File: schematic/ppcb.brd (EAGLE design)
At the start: 31.8 x 36.8 mm, 14 parts, among them U1 ATTINY*5, U2 LM211N

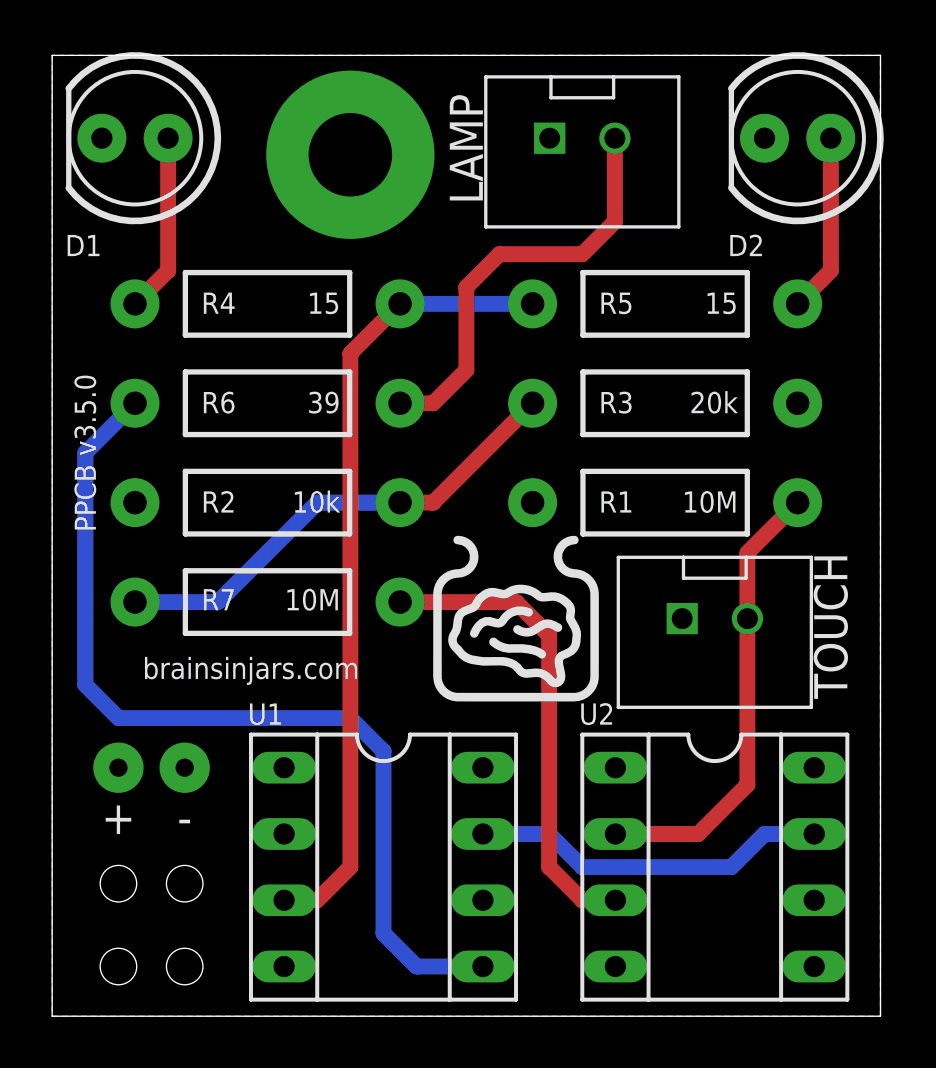
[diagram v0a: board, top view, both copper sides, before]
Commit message: Updated PCB to remove external analog comparator and make use of Timer/Counter-1 instead of Timer/Counter-0
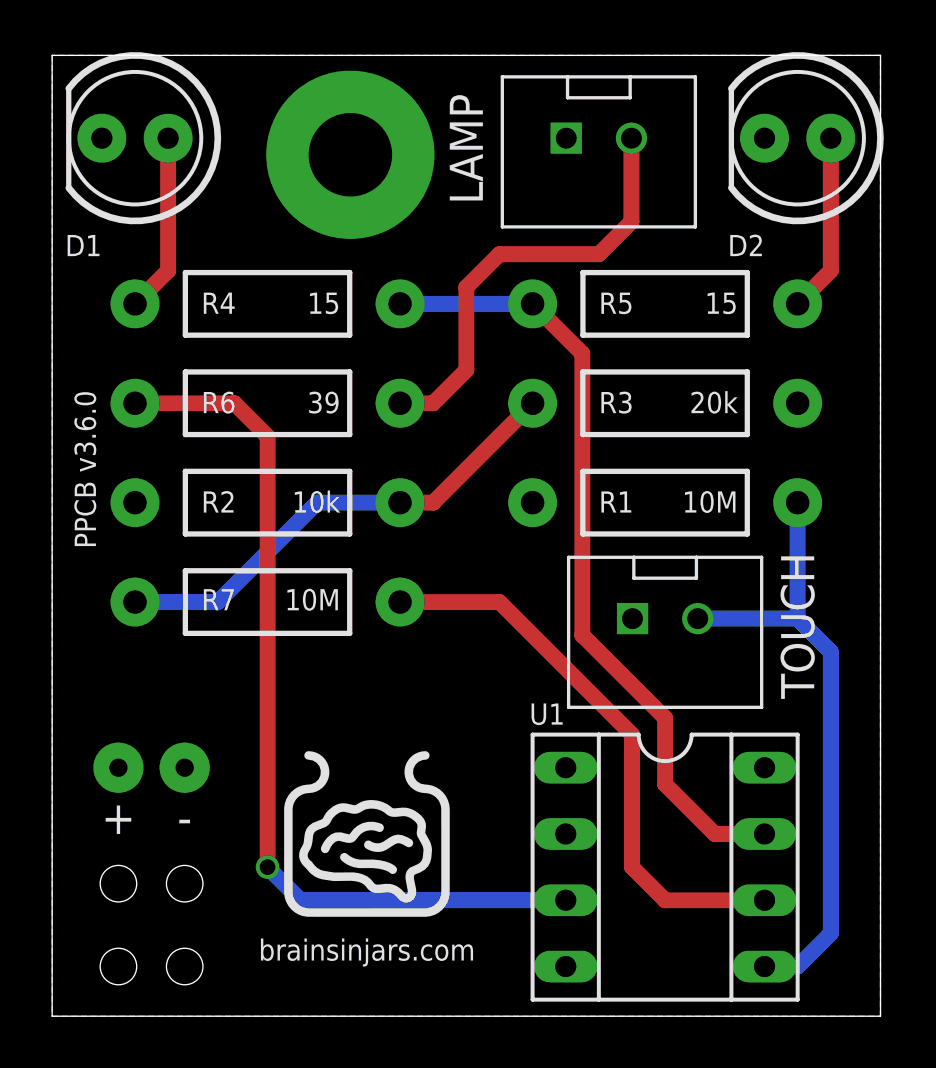
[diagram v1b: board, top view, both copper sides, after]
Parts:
- removed U2: LM211N, ic-package:SOCKET-08
- moved U1 10.8 mm to (23.5, 5.71)
- moved U$2 10.0 mm to (12.1, 6.99)
- moved SW 1.90 mm to (23.5, 15.2)
- moved LED 0.63 mm to (21.0, 33.7)
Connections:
- removed net TOUCH: U1.7, U2.7
- net N$1: now also U1.5; no longer U2.2
- net N$2: now also R7.P$2, U1.6; no longer R6.P$1, U1.5
- net N$7: now also R6.P$1, U1.3; no longer R7.P$2, U2.3
- net N$9: now also U1.7; no longer U1.3
- net V+: no longer U2.8
- net V-: no longer U2.1, U2.4
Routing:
- net N$7: track 18.2 -> 34.1 mm, vias 0 -> 1
- net TOUCH: track 13.8 -> 0.00 mm
- net N$2: track 35.4 -> 21.7 mm
- net N$1: track 17.5 -> 23.9 mm
- net N$3: track 16.2 -> 16.8 mm
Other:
- board text added: "PPCB v3.6.0"
- board text removed: "PPCB v3.5.0"
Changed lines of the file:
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@@
 <hole x="2.54" y="1.905" drill="1.4"/>
 <hole x="5.08" y="1.905" drill="1.4"/>
-<text x="7.62" y="13.335" size="0.8128" layer="21" font="vector" ratio="15" rot="R180" align="center">brainsinjars.com</text>
+<text x="12.065" y="2.54" size="0.8128" layer="21" font="vector" ratio="15" rot="R180" align="center">brainsinjars.com</text>
 <text x="16.51" y="31.115" size="1.27" layer="21" ratio="15" rot="R90">LAMP</text>
-<text x="29.21" y="17.78" size="1.27" layer="21" ratio="15" rot="R270">TOUCH</text>
-<text x="1.27" y="21.59" size="0.8128" layer="21" font="vector" ratio="15" rot="R90" align="center">PPCB v3.5.0</text>
+<text x="27.94" y="17.78" size="1.27" layer="21" ratio="15" rot="R270">TOUCH</text>
+<text x="1.27" y="20.955" size="0.8128" layer="21" font="vector" ratio="15" rot="R270" align="center">PPCB v3.6.0</text>
 </plain>
 <attributes>
@@
 </autorouter>
 <elements>
-<element name="LED" library="con-jst-xh" package="B2B-XH" value="02-JST" x="20.32" y="33.655"/>
-<element name="SW" library="con-jst-xh" package="B2B-XH" value="02-JST" x="25.4" y="15.24"/>
-<element name="U$2" library="brainsinjars" package="LOGO-1_4_IN" value="" x="17.78" y="15.24"/>
+<element name="LED" library="con-jst-xh" package="B2B-XH" value="02-JST" x="20.955" y="33.655"/>
+<element name="SW" library="con-jst-xh" package="B2B-XH" value="02-JST" x="23.495" y="15.24"/>
+<element name="U$2" library="brainsinjars" package="LOGO-1_4_IN" value="" x="12.065" y="6.985"/>
 <element name="R4" library="SparkFun-Resistors" package="AXIAL-0.4" value="15" x="8.255" y="27.305" smashed="yes">
 <attribute name="NAME" x="5.715" y="26.924" size="0.8128" layer="25" font="vector" ratio="15"/>
@@
 <attribute name="VALUE" x="25.3746" y="35.4584" size="1.27" layer="27" ratio="10" rot="R180"/>
 </element>
-<element name="U1" library="ic-package" package="SOCKET-08" value="ATTINY*5" x="12.7" y="5.715" smashed="yes" rot="R270">
-<attribute name="VALUE" x="12.192" y="8.763" size="1.27" layer="27" ratio="10" rot="R270"/>
-<attribute name="NAME" x="7.493" y="11.176" size="0.8128" layer="25" ratio="15"/>
-</element>
-<element name="U2" library="ic-package" package="SOCKET-08" value="LM211N" x="25.4" y="5.715" smashed="yes" rot="R270">
-<attribute name="VALUE" x="24.892" y="8.763" size="1.27" layer="27" ratio="10" rot="R270"/>
-<attribute name="NAME" x="20.193" y="11.176" size="0.8128" layer="25" ratio="15"/>
+<element name="U1" library="ic-package" package="SOCKET-08" value="ATTINY*5" x="23.495" y="5.715" smashed="yes" rot="R270">
+<attribute name="VALUE" x="22.987" y="8.763" size="1.27" layer="27" ratio="10" rot="R270"/>
+<attribute name="NAME" x="18.288" y="11.176" size="0.8128" layer="25" ratio="15"/>
 </element>
 <element name="R2" library="SparkFun-Resistors" package="AXIAL-0.4" value="10k" x="8.255" y="19.685" smashed="yes">
@@
 <via x="2.54" y="9.525" extent="1-16" drill="0.7" diameter="1.9304" alwaysstop="yes"/>
 <contactref element="R1" pad="P$1"/>
-<contactref element="U2" pad="8"/>
 <contactref element="U1" pad="8"/>
 <contactref element="R2" pad="P$1"/>
@@
 <via x="5.08" y="9.525" extent="1-16" drill="0.7" diameter="1.9304" shape="square" alwaysstop="yes"/>
 <contactref element="SW" pad="P$1"/>
-<contactref element="U2" pad="1"/>
-<contactref element="U2" pad="4"/>
 <contactref element="U1" pad="4"/>
 <contactref element="LED" pad="P$1"/>
@@
 <contactref element="D2" pad="K"/>
 <contactref element="R3" pad="P$2"/>
-</signal>
-<signal name="N$2">
-<contactref element="R6" pad="P$1"/>
-<contactref element="U1" pad="5"/>
-<wire x1="3.175" y1="23.495" x2="1.27" y2="21.59" width="0.6096" layer="16"/>
-<wire x1="1.27" y1="21.59" x2="1.27" y2="12.7" width="0.6096" layer="16"/>
-<wire x1="1.27" y1="12.7" x2="2.54" y2="11.43" width="0.6096" layer="16"/>
-<wire x1="2.54" y1="11.43" x2="11.43" y2="11.43" width="0.6096" layer="16"/>
-<wire x1="11.43" y1="11.43" x2="12.7" y2="10.16" width="0.6096" layer="16"/>
-<wire x1="12.7" y1="10.16" x2="12.7" y2="3.175" width="0.6096" layer="16"/>
-<wire x1="12.7" y1="3.175" x2="13.97" y2="1.905" width="0.6096" layer="16"/>
-<wire x1="13.97" y1="1.905" x2="16.51" y2="1.905" width="0.6096" layer="16"/>
 </signal>
 <signal name="N$3">
@@
 <wire x1="15.875" y1="24.765" x2="14.605" y2="23.495" width="0.6096" layer="1"/>
 <wire x1="14.605" y1="23.495" x2="13.335" y2="23.495" width="0.6096" layer="1"/>
-<wire x1="21.57" y1="33.655" x2="21.57" y2="30.46" width="0.6096" layer="1"/>
-<wire x1="21.57" y1="30.46" x2="20.32" y2="29.21" width="0.6096" layer="1"/>
-<wire x1="20.32" y1="29.21" x2="17.145" y2="29.21" width="0.6096" layer="1"/>
+<wire x1="22.205" y1="33.655" x2="22.205" y2="30.46" width="0.6096" layer="1"/>
+<wire x1="22.205" y1="30.46" x2="20.955" y2="29.21" width="0.6096" layer="1"/>
+<wire x1="20.955" y1="29.21" x2="17.145" y2="29.21" width="0.6096" layer="1"/>
 </signal>
 <signal name="N$4">
@@
 <contactref element="R5" pad="P$1"/>
 <wire x1="18.415" y1="27.305" x2="13.335" y2="27.305" width="0.6096" layer="16"/>
-<wire x1="10.16" y1="4.445" x2="11.43" y2="5.715" width="0.6096" layer="1"/>
-<wire x1="11.43" y1="5.715" x2="11.43" y2="25.4" width="0.6096" layer="1"/>
-<wire x1="11.43" y1="25.4" x2="13.335" y2="27.305" width="0.6096" layer="1"/>
-<contactref element="U1" pad="3"/>
-<wire x1="8.89" y1="4.445" x2="10.16" y2="4.445" width="0.6096" layer="1"/>
-</signal>
-<signal name="TOUCH">
-<contactref element="U2" pad="7"/>
 <contactref element="U1" pad="7"/>
-<wire x1="29.21" y1="6.985" x2="27.305" y2="6.985" width="0.6096" layer="16"/>
-<wire x1="27.305" y1="6.985" x2="26.035" y2="5.715" width="0.6096" layer="16"/>
-<wire x1="26.035" y1="5.715" x2="20.32" y2="5.715" width="0.6096" layer="16"/>
-<wire x1="20.32" y1="5.715" x2="19.05" y2="6.985" width="0.6096" layer="16"/>
-<wire x1="19.05" y1="6.985" x2="16.51" y2="6.985" width="0.6096" layer="16"/>
+<wire x1="18.415" y1="27.305" x2="20.32" y2="25.4" width="0.6096" layer="1"/>
+<wire x1="20.32" y1="25.4" x2="20.32" y2="14.605" width="0.6096" layer="1"/>
+<wire x1="20.32" y1="14.605" x2="23.495" y2="11.43" width="0.6096" layer="1"/>
+<wire x1="23.495" y1="11.43" x2="23.495" y2="8.89" width="0.6096" layer="1"/>
+<wire x1="23.495" y1="8.89" x2="25.4" y2="6.985" width="0.6096" layer="1"/>
+<wire x1="25.4" y1="6.985" x2="27.305" y2="6.985" width="0.6096" layer="1"/>
 </signal>
 <signal name="N$1">
 <contactref element="SW" pad="P$2"/>
 <contactref element="R1" pad="P$2"/>
-<contactref element="U2" pad="2"/>
-<wire x1="26.65" y1="15.24" x2="26.65" y2="17.76" width="0.6096" layer="1"/>
-<wire x1="26.65" y1="17.76" x2="28.575" y2="19.685" width="0.6096" layer="1"/>
-<wire x1="26.65" y1="15.24" x2="26.65" y2="8.87" width="0.6096" layer="1"/>
-<wire x1="26.65" y1="8.87" x2="24.765" y2="6.985" width="0.6096" layer="1"/>
-<wire x1="24.765" y1="6.985" x2="21.59" y2="6.985" width="0.6096" layer="1"/>
+<contactref element="U1" pad="5"/>
+<wire x1="27.305" y1="1.905" x2="28.575" y2="1.905" width="0.6096" layer="16"/>
+<wire x1="28.575" y1="1.905" x2="29.845" y2="3.175" width="0.6096" layer="16"/>
+<wire x1="29.845" y1="3.175" x2="29.845" y2="13.97" width="0.6096" layer="16"/>
+<wire x1="29.845" y1="13.97" x2="28.575" y2="15.24" width="0.6096" layer="16"/>
+<wire x1="28.575" y1="15.24" x2="24.745" y2="15.24" width="0.6096" layer="16"/>
+<wire x1="28.575" y1="19.685" x2="28.575" y2="15.24" width="0.6096" layer="16"/>
 </signal>
 <signal name="N$5">
@@
 <wire x1="10.16" y1="19.685" x2="13.335" y2="19.685" width="0.6096" layer="16"/>
 </signal>
+<signal name="N$2">
+<contactref element="U1" pad="6"/>
+<contactref element="R7" pad="P$2"/>
+<wire x1="13.335" y1="15.875" x2="17.145" y2="15.875" width="0.6096" layer="1"/>
+<wire x1="17.145" y1="15.875" x2="22.225" y2="10.795" width="0.6096" layer="1"/>
+<wire x1="22.225" y1="10.795" x2="22.225" y2="5.715" width="0.6096" layer="1"/>
+<wire x1="22.225" y1="5.715" x2="23.495" y2="4.445" width="0.6096" layer="1"/>
+<wire x1="23.495" y1="4.445" x2="27.305" y2="4.445" width="0.6096" layer="1"/>
+</signal>
 <signal name="N$7">
-<contactref element="R7" pad="P$2"/>
-<contactref element="U2" pad="3"/>
-<wire x1="21.59" y1="4.445" x2="20.32" y2="4.445" width="0.6096" layer="1"/>
-<wire x1="20.32" y1="4.445" x2="19.05" y2="5.715" width="0.6096" layer="1"/>
-<wire x1="19.05" y1="5.715" x2="19.05" y2="14.605" width="0.6096" layer="1"/>
-<wire x1="19.05" y1="14.605" x2="17.78" y2="15.875" width="0.6096" layer="1"/>
-<wire x1="17.78" y1="15.875" x2="13.335" y2="15.875" width="0.6096" layer="1"/>
+<contactref element="R6" pad="P$1"/>
+<contactref element="U1" pad="3"/>
+<wire x1="19.685" y1="4.445" x2="9.525" y2="4.445" width="0.6096" layer="16"/>
+<wire x1="9.525" y1="4.445" x2="8.255" y2="5.715" width="0.6096" layer="16"/>
+<wire x1="8.255" y1="5.715" x2="8.255" y2="22.225" width="0.6096" layer="1"/>
+<wire x1="8.255" y1="22.225" x2="6.985" y2="23.495" width="0.6096" layer="1"/>
+<wire x1="6.985" y1="23.495" x2="3.175" y2="23.495" width="0.6096" layer="1"/>
+<via x="8.255" y="5.715" extent="1-16" drill="0.6" shape="octagon"/>
 </signal>
 </signals>
